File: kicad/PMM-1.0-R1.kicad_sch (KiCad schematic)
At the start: 6 parts, among them U11 TPS22917DBV, U2 BQ25895RTW, U4 BQ27441-G1, U6 TPS61089, U9 STM32C031C4T6

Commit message: add simulations
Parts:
- added C10, C11, C12, C8, C9: 47uF, symbol Device:C_Small
- added C2: 0.1uF, symbol Device:C_Small
- added C3, C5: 100nF, symbol Device:C_Small
- added C4: 10uF, symbol Device:C_Small
- added C6: 560pF, symbol Device:C_Small
- added C7: 24pF, symbol Device:C_Small
- added L1: 470nH, symbol Device:L_Ferrite_Small
- added R1: 309k, symbol Device:R_Small_US
- added R2: 133k, symbol Device:R_Small_US
- added R3: 28.7k, symbol Device:R_Small_US
- added R4: 240k, symbol Device:R_Small_US
- added R5: 76.8k, symbol Device:R_Small_US
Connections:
- net GND: now also U6.5 (GND), C10.2, C11.2, C12.2, C3.2, C4.2, C5.2, C6.2, C7.2, C8.2, C9.2, R2.2, R5.2
- net at U6.1 (FSW): now also R1.2
- net at U6.10 (BOOT): now also C2.2
- net at U6.11 (SW): now also C2.1, L1.2, R1.1
- net at U6.2 (VCC): now also U6.7 (EN), C4.1
- net at U6.3 (FB): now also R4.2, R5.1
- net at U6.4 (COMP): now also C7.1, R3.1
- net at U6.6 (VOUT): now also C5.1, C8.1, C9.1, R4.1
- net at U6.8 (ILIM): now also R2.1
- net at U6.9 (VIN): now also C10.1, C11.1, C12.1, C3.1, L1.1
- new net: C6.1, R3.2
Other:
- note added: "3v-4.35v"
- note added: "5v @ 2A"
- moved on the sheet: C1, U11, U2, U4, U6

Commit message: changes
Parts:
- added C13: Cl, symbol Device:C_Small
- added C14: Ct, symbol Device:C_Small
- added C15: Cin, symbol Device:C_Small
- added R6: Rqod, symbol Device:R_Small_US
- added R7: 0.010 1%, symbol Device:R_Small_US
- added U1: TLV75733PDBV, Package_TO_SOT_SMD:SOT-23-5, symbol Regulator_Linear:TLV75733PDBV
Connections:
- net GND: now also U11.2 (GND), C13.2, C15.2
- net at U11.1 (VIN): now also C14.1, C15.1
- net at U11.4 (CT): now also C14.2
- net at U11.5 (QOD): now also R6.2
- net at U11.6 (VOUT): now also C13.1, R6.1
- net BAT: now reaches U4.6 (BAT)
- net BAT: now also U4.8 (SRP), R7.2
- net VSYS: now reaches U4.7 (SRN)
- net VSYS: now also R7.1
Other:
- note added: "2.7Vin Duty Cycle 48.31% Efficiency 93.7% Frequency 496.71kHz Pout 10W Mode BOOST CCM Vout p-p 38.09mV Vout Actual 5V Vout tolerance 4.17% Vin 2.7V Iout 2A"
- note added: "5v"
- moved on the sheet: U11

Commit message: updates
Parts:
- added C16: 1uF, symbol Device:C_Small
- added R8: 10k, symbol Device:R_Small_US
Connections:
- net GND: now also U2.17 (PGND), U2.18 (PGND), U2.25 (PGND), R8.2
- net at U4.10 (BIN): now also R8.1
- net BAT renamed PACK+
- net PACK+: now also C16.1
- new net PACK-: C16.2
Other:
- moved on the sheet: C1, C10, C11, C12, C13, C14, C15, C2, C3, C4, C5, C6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

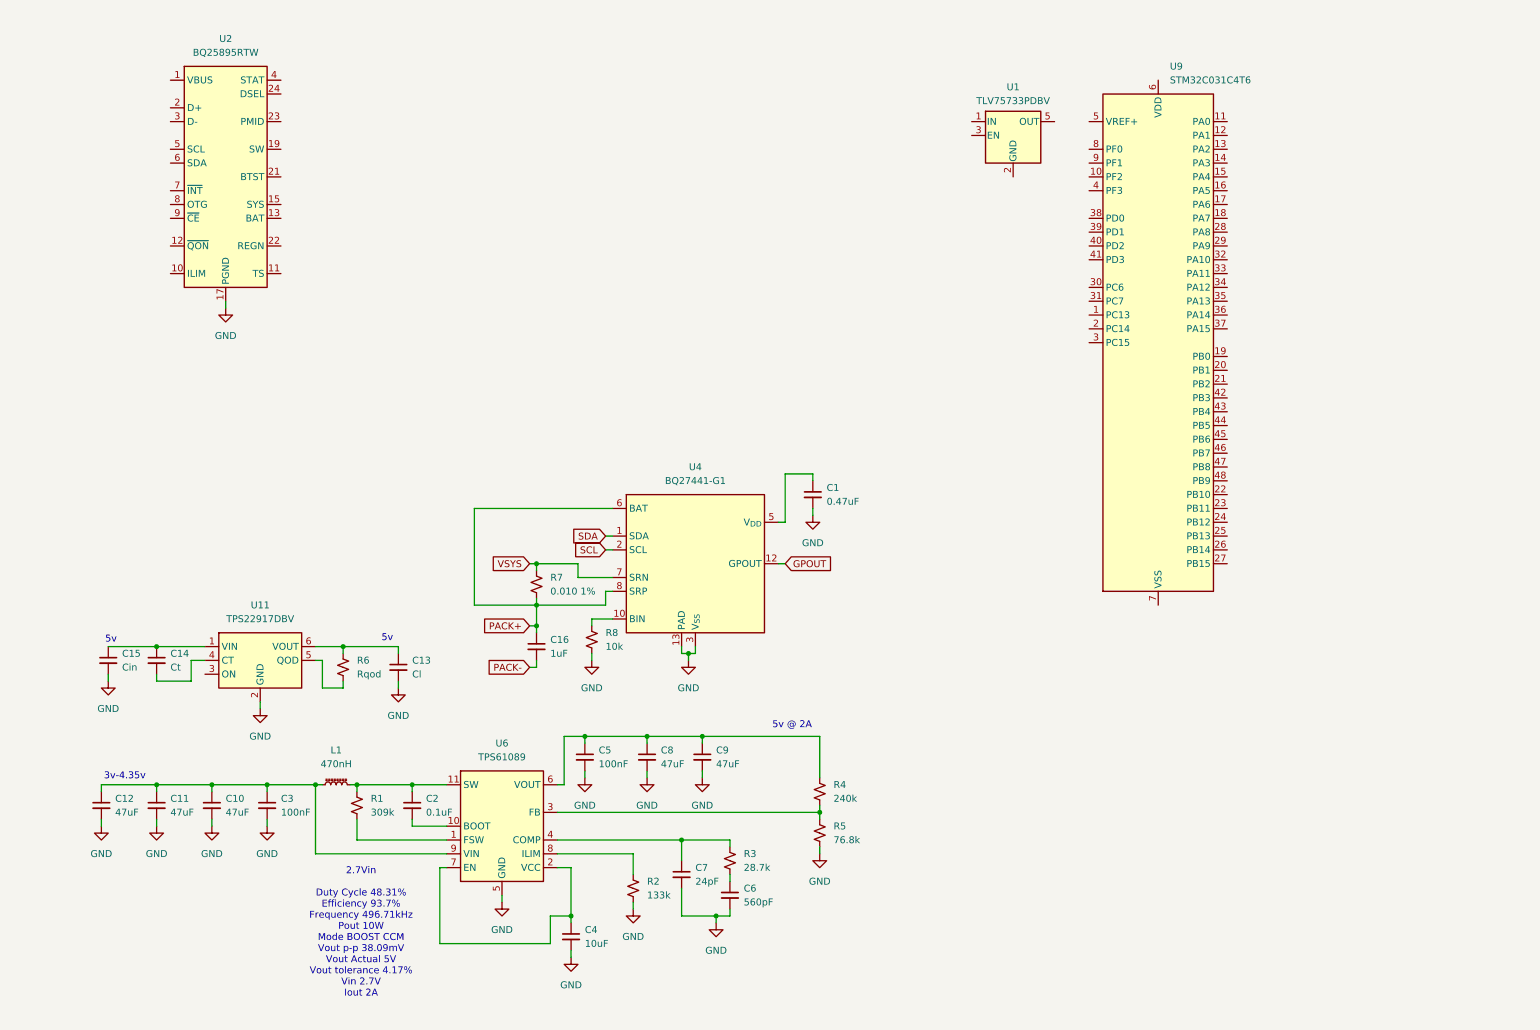
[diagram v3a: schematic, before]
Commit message: 3.3v regulator
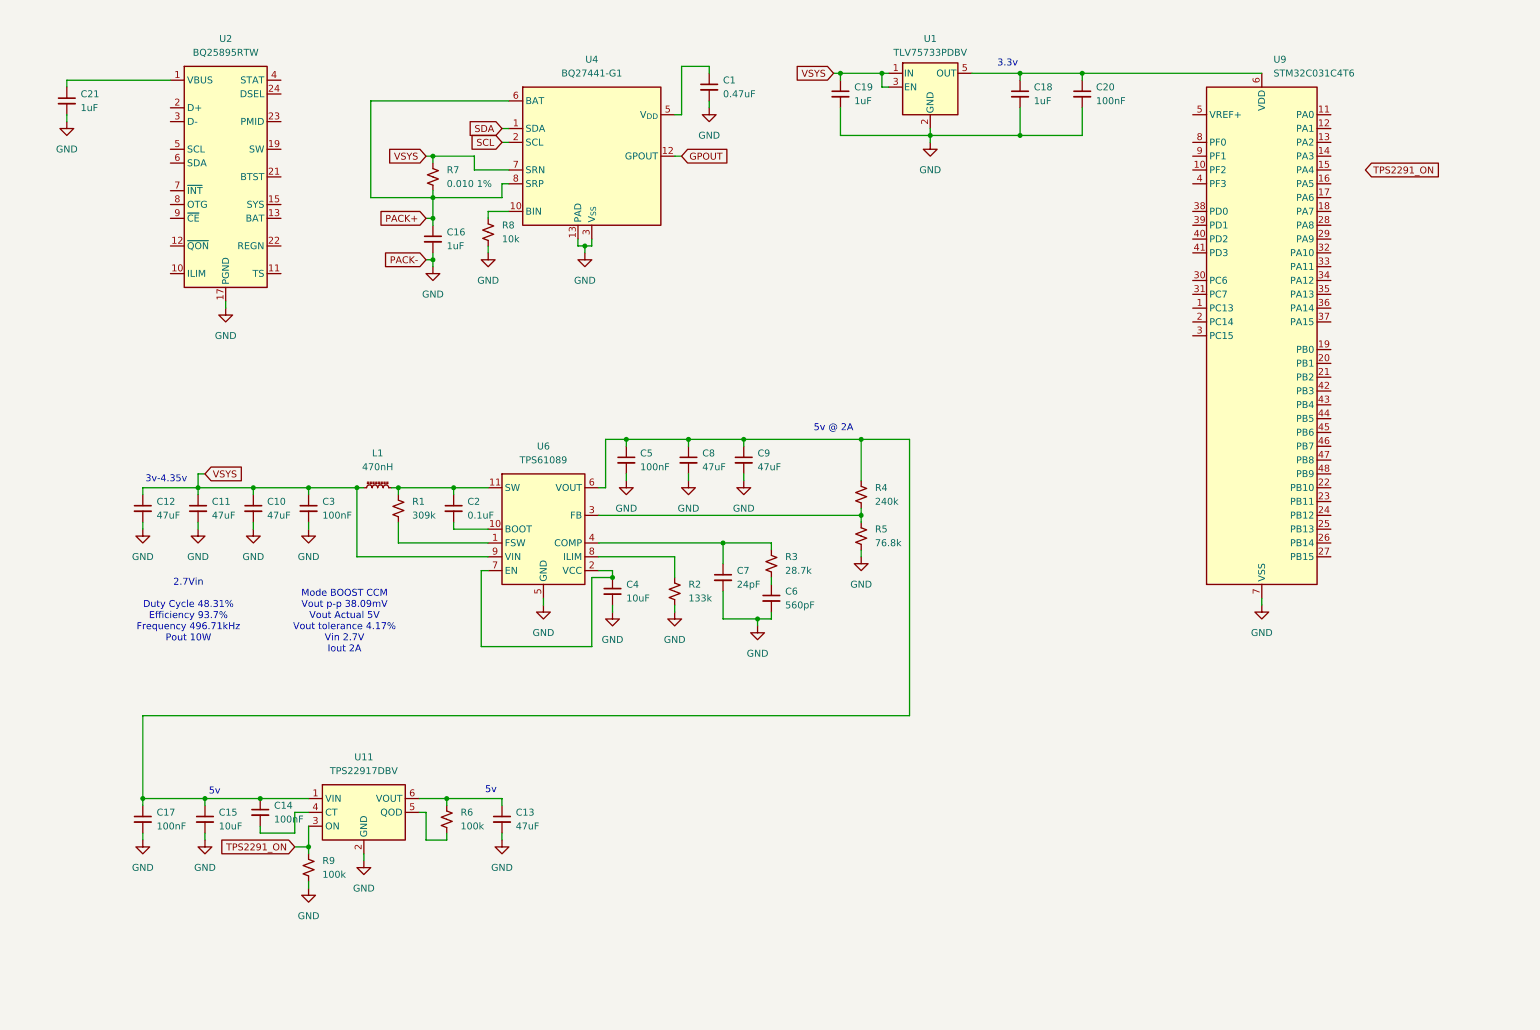
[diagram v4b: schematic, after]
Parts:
- added C17, C20: 100nF, symbol Device:C_Small
- added C18, C19, C21: 1uF, symbol Device:C_Small
- added R9: 100k, symbol Device:R_Small_US
- C13: value Cl -> 47uF
- C14: value Ct -> 100nF
- C15: value Cin -> 10uF
- R6: value Rqod -> 100k
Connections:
- net PACK- is gone; now on net GND: C16.2
- net GND: now also U1.2 (GND), U9.7 (VSS), C17.2, C18.2, C19.2, C20.2, C21.2, R9.2
- net VSYS: now also C10.1, C11.1, C12.1, C3.1, L1.1, U1.1 (IN), U1.3 (EN), U6.9 (VIN), C19.1
- net at C14.1, C15.1, U11.1 (VIN): now also C5.1, C8.1, C9.1, R4.1, U6.6 (VOUT), C17.1
- net TPS2291_ON: now reaches U11.3 (ON)
- net TPS2291_ON: now also R9.1
- net at U1.5 (OUT): now also U9.6 (VDD), C18.1, C20.1
- net at U2.1 (VBUS): now also C21.1
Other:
- note added: "2.7Vin Duty Cycle 48.31% Efficiency 93.7% Frequency 496.71kHz Pout 10W"
- note added: "3.3v"
- note added: "Mode BOOST CCMr Vout p-p 38.09mVr Vout Actual 5Vr Vout tolerance 4.17%r Vin 2.7Vr Iout 2A"
- note removed: "2.7Vin Duty Cycle 48.31% Efficiency 93.7% Frequency 496.71kHz Pout 10W Mode BOOST CCM Vout p-p 38.09mV Vout Actual 5V Vout tolerance 4.17% Vin 2.7V Iout 2A"
- moved on the sheet: C1, C10, C11, C12, C13, C14, C15, C16, C2, C3, C4, C5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

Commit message: fix aux 3.3v regulator
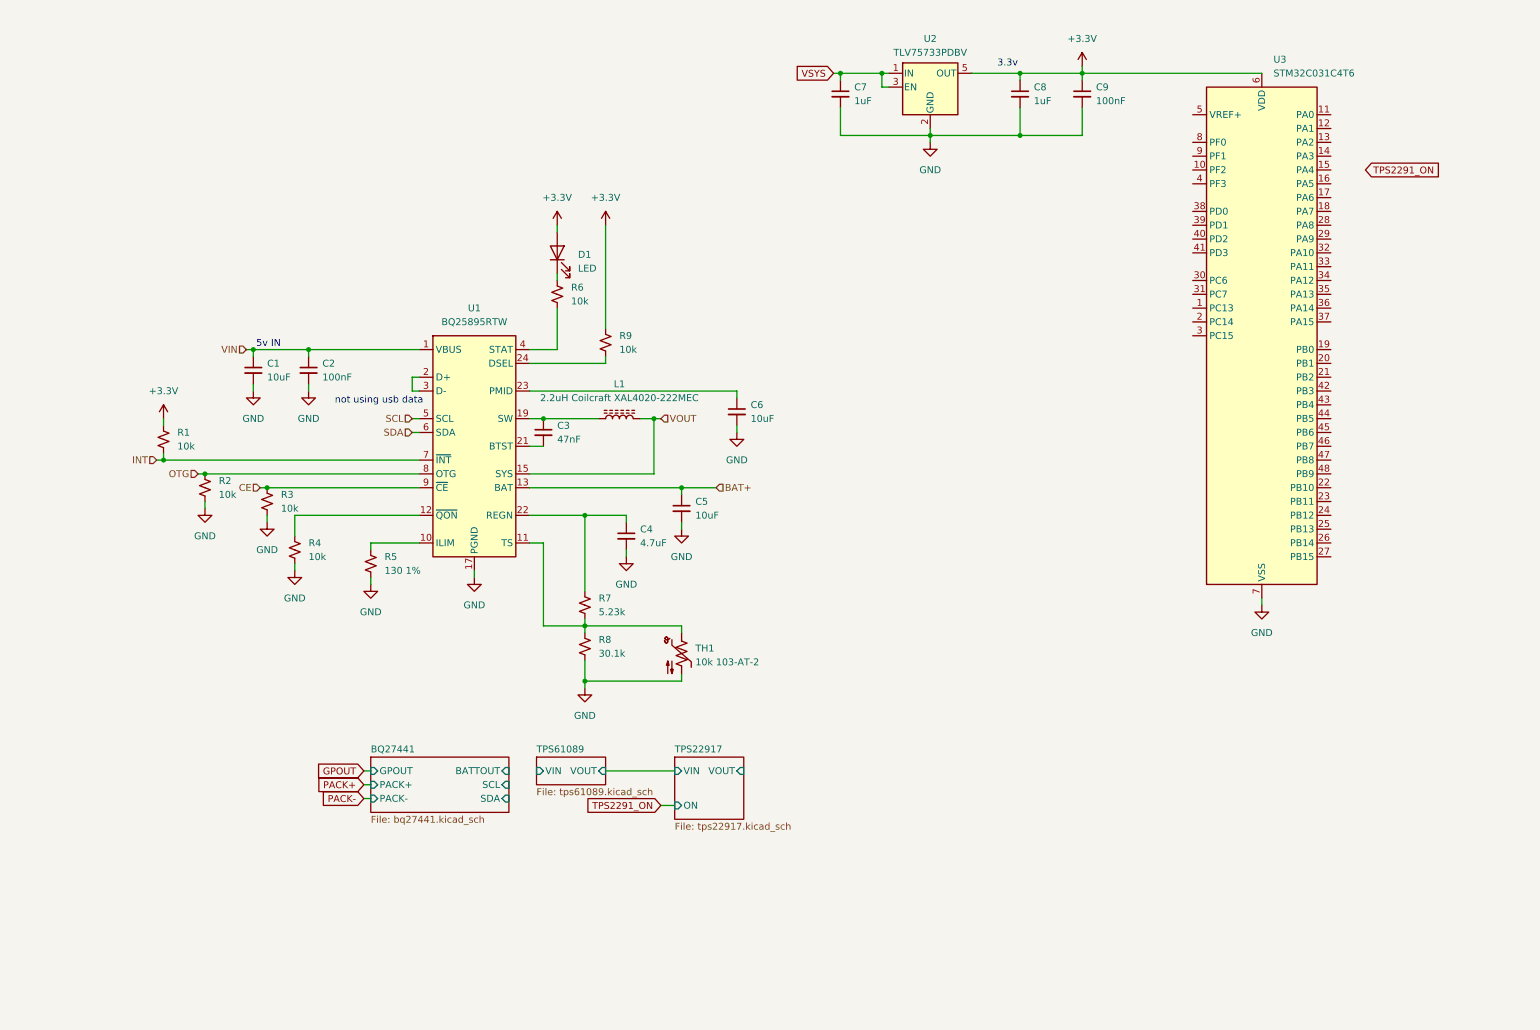
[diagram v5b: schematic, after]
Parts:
- removed C1: 0.47uF, symbol Device:C_Small
- removed C10, C11, C12, C13, C8, C9: 47uF, symbol Device:C_Small
- removed C14, C17: 100nF, symbol Device:C_Small
- removed C15: 10uF, symbol Device:C_Small
- removed C16: 1uF, symbol Device:C_Small
- removed C7: 24pF, symbol Device:C_Small
- removed L1: 470nH, symbol Device:L_Ferrite_Small
- removed U11: TPS22917DBV, Package_TO_SOT_SMD:SOT-23-6, symbol Power_Management:TPS22917DBV
- removed U4: BQ27441-G1, Package_SON:Texas_S-PDSO-N12, symbol Battery_Management:BQ27441-G1
- removed U6: TPS61089, Package_DFN_QFN:Texas_VQFN-RNR0011A-11, symbol Regulator_Switching:TPS61089
- added D1: LED, symbol Device:LED
- added L1: 2.2uH Coilcraft XAL4020-222MEC, Inductor_SMD:L_Coilcraft_XxL4020, symbol Device:L_Ferrite
- added TH1: 10k 103-AT-2, symbol Device:Thermistor_NTC_US
- C1: renamed from C21; value 1uF -> 10uF
- C2: value 0.1uF -> 100nF
- C3: value 100nF -> 47nF
- C4: value 10uF -> 4.7uF
- C5: value 100nF -> 10uF
- C6: value 560pF -> 10uF
- R1: value 309k -> 10k
- R2: value 133k -> 10k
- R3: value 28.7k -> 10k
- R4: value 240k -> 10k
- R5: value 76.8k -> 130 1%
- R6, R9: value 100k -> 10k
- R7: value 0.010 1% -> 5.23k
- R8: value 10k -> 30.1k
- renumbered C19 to C7, C18 to C8, C20 to C9, U2 to U1, U1 to U2, U9 to U3
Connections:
- net GND: now also C2.2, R3.2, R4.2, TH1.2; no longer C3.2, R9.2
- net PACK+: no longer R7.2
- net SCL: now also U1.5 (SCL)
- net SDA: now also U1.6 (SDA)
- net TPS2291_ON: no longer R9.1
- net VSYS: no longer C3.1, R7.1
- net +3.3V: now reaches R1.1
- net +3.3V: now also C8.1, C9.1, R9.1, U2.5 (OUT), U3.6 (VDD), D1.2 (A); no longer C2.1
- net CE: now reaches R3.1
- net CE: now also U1.9 (~{CE})
- net at R4.1: now also U1.12 (~{QON}); no longer C5.1
- net at R8.1: now also R7.2, U1.11 (TS), TH1.1
- net at C6.1: now also U1.23 (PMID); no longer R3.2
- net at R6.2: now also U1.4 (STAT)
- net at R6.1: now also D1.1 (K)
- net at R5.1: now also U1.10 (ILIM); no longer R4.2
- net INT: now reaches R1.2
- net INT: now also U1.7 (~{INT})
- net at C4.1: now also R7.1, U1.22 (REGN)
- net OTG: now reaches R2.1
- net OTG: now also U1.8 (OTG)
- net VIN: now reaches C1.1, U1.1 (VBUS)
- net VIN: now also C2.1
- net BAT+: now reaches U1.13 (BAT), U1.14 (BAT)
- net BAT+: now also C5.1
- net VOUT: now reaches U1.15 (SYS), U1.16 (SYS)
- net VOUT: now also L1.2
- net at U1.19 (SW), U1.20 (SW): now also C3.1, L1.1
- net at U1.2 (D+): now also U1.3 (D-)
- net at U1.21 (BTST): now also C3.2
- net at U1.24 (DSEL): now also R9.2
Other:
- added sheet BQ27441 (bq27441.kicad_sch)
- added sheet TPS22917 (tps22917.kicad_sch)
- added sheet TPS61089 (tps61089.kicad_sch)
- note added: "5v IN"
- note added: "not using usb data"
- note removed: "2.7Vin Duty Cycle 48.31% Efficiency 93.7% Frequency 496.71kHz Pout 10W"
- note removed: "3v-4.35v"
- note removed: "5v"
- note removed: "5v @ 2A"
- note removed: "Mode BOOST CCMr Vout p-p 38.09mVr Vout Actual 5Vr Vout tolerance 4.17%r Vin 2.7Vr Iout 2A"
- moved on the sheet: C1, U1

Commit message: add tlv 3.3v sheet
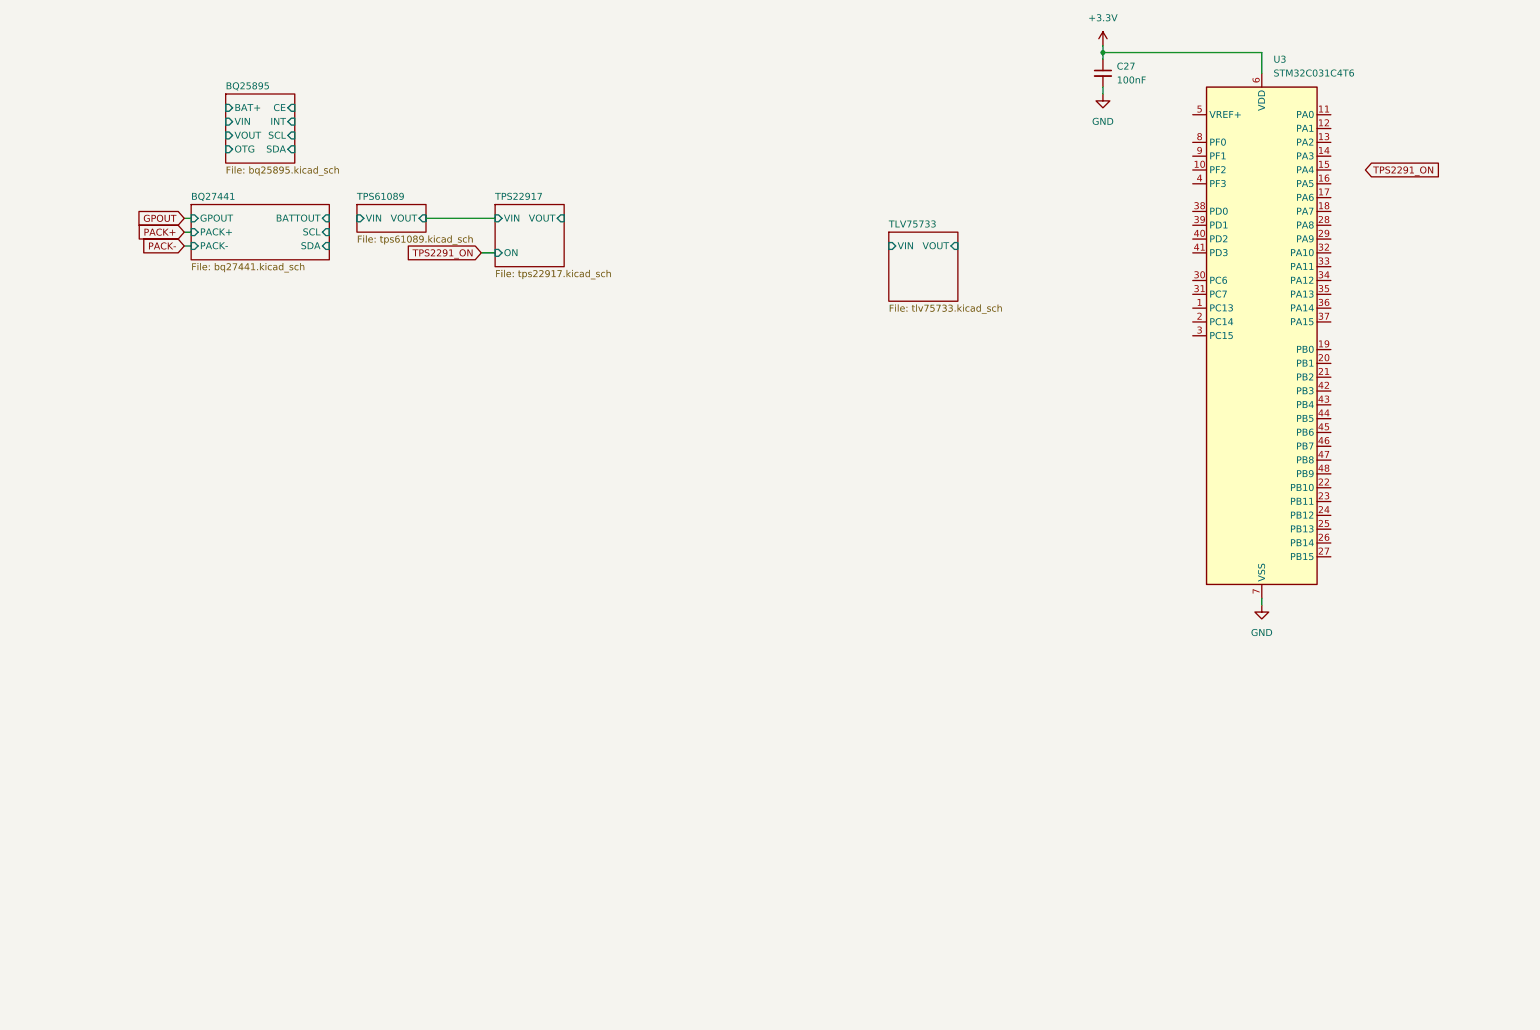
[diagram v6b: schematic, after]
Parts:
- removed C1, C5, C6: 10uF, symbol Device:C_Small
- removed C2, C9: 100nF, symbol Device:C_Small
- removed C3: 47nF, symbol Device:C_Small
- removed C4: 4.7uF, symbol Device:C_Small
- removed C7, C8: 1uF, symbol Device:C_Small
- removed D1: LED, symbol Device:LED
- removed L1: 2.2uH Coilcraft XAL4020-222MEC, Inductor_SMD:L_Coilcraft_XxL4020, symbol Device:L_Ferrite
- removed R1, R2, R3, R4, R6, R9: 10k, symbol Device:R_Small_US
- removed R5: 130 1%, symbol Device:R_Small_US
- removed R7: 5.23k, symbol Device:R_Small_US
- removed R8: 30.1k, symbol Device:R_Small_US
- removed TH1: 10k 103-AT-2, symbol Device:Thermistor_NTC_US
- removed U1: BQ25895RTW, Package_DFN_QFN:Texas_RTW_WQFN-24-1EP_4x4mm_P0.5mm_EP2.7x2.7mm_ThermalVias, symbol Battery_Management:BQ25895RTW
- removed U2: TLV75733PDBV, Package_TO_SOT_SMD:SOT-23-5, symbol Regulator_Linear:TLV75733PDBV
- added C27: 100nF, symbol Device:C_Small
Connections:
- net +3.3V: now also C27.1
- net GND: now also C27.2
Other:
- added sheet BQ25895 (bq25895.kicad_sch)
- added sheet TLV75733 (tlv75733.kicad_sch)
- note removed: "3.3v"
- note removed: "5v IN"
- note removed: "not using usb data"
